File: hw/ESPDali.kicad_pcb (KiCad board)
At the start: 2 copper layers, 34 x 46 mm, 52 parts, among them J1 2pin 3.5mm terminal block, J2 2pin 3.5mm terminal block, J3 2.54mm pin header, Q1 BCX56-16, Q2 SMBT2222A, Q3 BCX56-16, SW1 SW_Push, SW2 SW_Push, U1 LM27313XMF, U2 TLP185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

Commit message: Footprint fixes to PCB
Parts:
- removed C10, C11: 1n, Capacitor_SMD:C_0603_1608Metric
- removed R15, R16: 470R, Resistor_SMD:R_0603_1608Metric
- removed SW1, SW2: SW_Push, Button_Switch_SMD:SW_Push_SPST_NO_Alps_SKRK
- C9, R13: moved to F.Cu
- J3: footprint Connector_PinHeader_2.54mm:PinHeader_1x03_P2.54mm_Vertical -> Connector_PinHeader_2.54mm:PinHeader_1x05_P2.54mm_Vertical
- R2: value 100k -> 330
- R6: value 13.3k -> 13k
- U3: value MCP1804x-3302xDB -> SPX2920M3-3.3_SOT223
- moved C9 7.39 mm to (163.0, 111.5)
- moved R13 7.34 mm to (161.4, 111.5)
- moved C5 7.13 mm to (164.4, 111.3)
- moved C6 6.86 mm to (164.2, 114.6)
- moved J3 5.08 mm to (135.6, 97.5)
- moved R14 4.97 mm to (142.2, 103.7)
- moved U3 4.09 mm to (158.8, 112.6), turned to 180 degrees
- moved C4 2.25 mm to (143.4, 84.9), turned to 90 degrees
- moved R4 0.30 mm to (155.5, 87.7)
- moved C7 0.21 mm to (161.4, 114.7)
- moved R2 0.17 mm to (144.0, 103.7)
- moved C8 0.16 mm to (163.0, 114.7)
- moved R11 0.12 mm to (145.7, 103.7)
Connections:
- C9 pad 1: /RESET -> /EN
- D2 pad 2: Net-(J2-Pin_1) -> GNDPWR
- D2 pad 4: GNDPWR -> Net-(J2-Pin_1)
- R13 pad 2: /RESET -> /EN
- U3 pad 1: +3V3 -> /VIN
- U3 pad 3: /VIN -> +3V3
- U5 pad 24: /LED -> unconnected-(U5-IO2-Pad24)
- U5 pad 3: /RESET -> /EN
- U5 pad 36: unconnected-(U5-IO22-Pad36) -> /LED
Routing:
- net /EN: track 0.00 -> 40.2 mm
- net /RESET: track 17.6 -> 0.00 mm, vias 1 -> 0
- net /LED: track 17.5 -> 4.62 mm
- net +3V3: track 39.6 -> 51.4 mm
- net /BOOT: track 25.6 -> 15.3 mm
- net Net-(J2-Pin_1): track 10.3 -> 16.3 mm
- net /RXD: track 8.03 -> 13.3 mm
- net GNDPWR: track 18.4 -> 23.6 mm
- net /TXD: track 7.50 -> 12.2 mm
- net GND: track 40.1 -> 43.9 mm, vias 41 -> 34
- net Net-(C11-Pad1): track 3.34 -> 0.00 mm, vias 1 -> 0
- net Net-(C10-Pad1): track 2.70 -> 0.00 mm, vias 1 -> 0
- net /VIN: track 52.9 -> 52.1 mm, vias 0 -> 2
- net Net-(J2-Pin_2): track 12.4 -> 13.0 mm
- net /BOOST_OUT: track 14.6 -> 14.9 mm, vias 2 -> 5
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- added copper zone on B.Cu, net /BOOST_OUT
- added copper zone on F.Cu, net /BOOST_OUT
- added copper zone on B.Cu, net /DALI_DATA
- added copper zone on F.Cu, net /DALI_DATA
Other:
- board text added: "5-18V"
- board text added: "ESP32 DALI"
- board text added: "GND RXD TXD BOOT EN"
- board text removed: "5-14V"
- board text removed: "BOOT"
- board text removed: "EN"
- board text removed: "EPS32 DALI"
- board text removed: "GND RXD TXD"

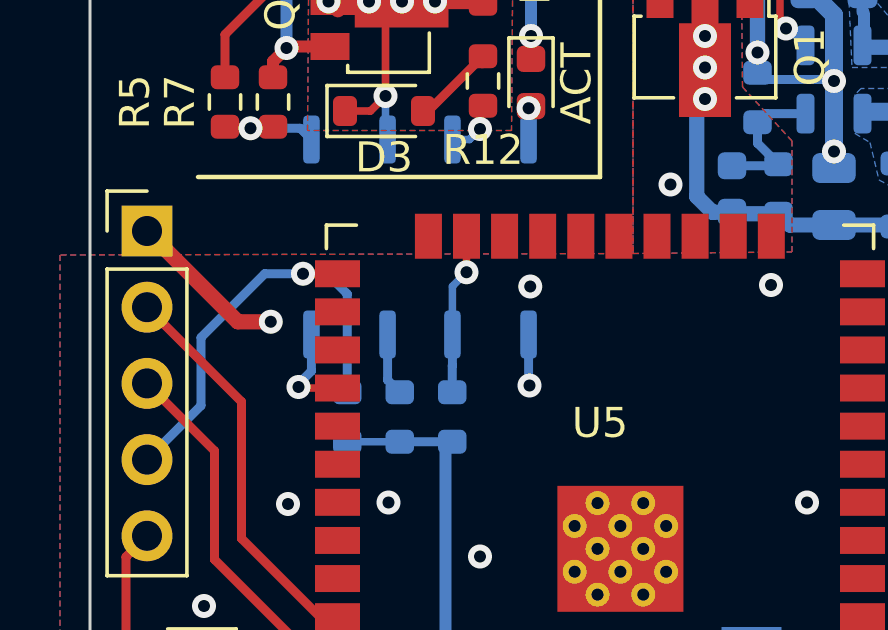
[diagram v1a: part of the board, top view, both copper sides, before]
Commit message: Update to KiCAD 8
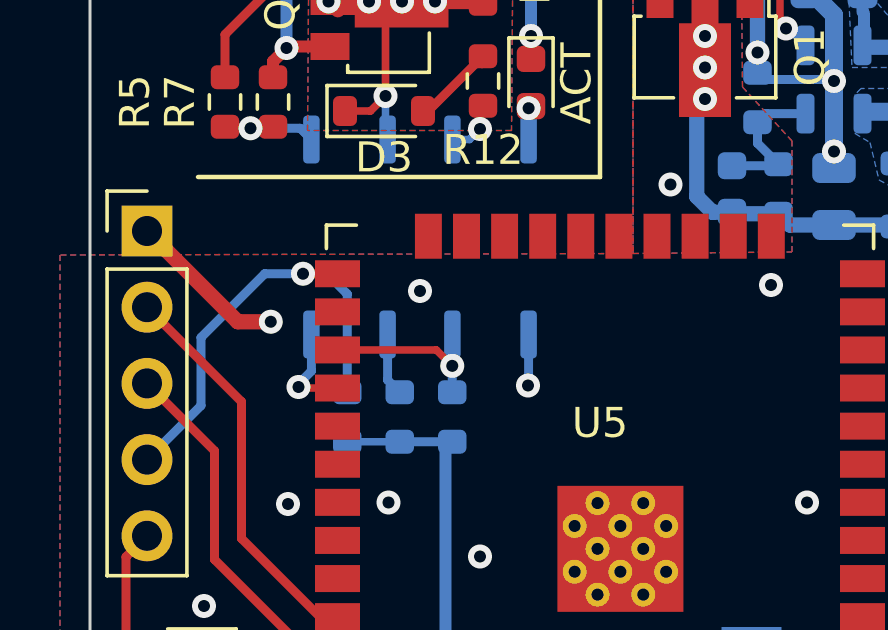
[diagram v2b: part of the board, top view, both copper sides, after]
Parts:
- U3: value SPX2920M3-3.3_SOT223 -> MCP1703A-330
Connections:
- U5 pad 23: /DALI_RX -> unconnected-(U5-IO15-Pad23)
- U5 pad 27: unconnected-(U5-IO16-Pad27) -> /DALI_RX
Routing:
- net /DALI_RX: track 5.40 -> 5.97 mm
